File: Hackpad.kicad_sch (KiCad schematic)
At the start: 46 parts, among them Q1 SW_Push, U1 MOUDLE-SEEEDUINO-XIAO

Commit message: Rev 1.0
idk
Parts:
- RGB15: footprint LED_SMD:LED_SK6812MINI_PLCC4_3.5x3.5mm_P1.75mm -> footprints:SK6812MINI-E_fixed
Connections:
- net GND: now also U1.13 (GND)
- net LED: now also U1.8 (PB09_A7_D7_RX); no longer U1.6 (PA9_A5_D5_SCL)
- no-connect marks 0 -> 3
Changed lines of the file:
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@@
 		(color 0 0 0 0)
 	)
+	(no_connect
+		(at 281.94 165.1)
+	)
+	(no_connect
+		(at 21.59 86.36)
+	)
+	(no_connect
+		(at 21.59 83.82)
+	)
 	(wire
 		(pts
@@
 		)
 	)
-	(global_label "LED"
+	(global_label "COL3"
 		(shape input)
-		(at 21.59 83.82 180)
+		(at 132.08 20.32 180)
 		(fields_autoplaced yes)
 		(effects
@@
 		)
 		(property "Intersheetrefs" "${INTERSHEET_REFS}"
-			(at 15.1577 83.82 0)
+			(at 124.2567 20.32 0)
 			(hide yes)
 			(show_name no)
@@
 	(global_label "COL3"
 		(shape input)
-		(at 132.08 20.32 180)
+		(at 21.59 76.2 180)
 		(fields_autoplaced yes)
 		(effects
@@
 		)
 		(property "Intersheetrefs" "${INTERSHEET_REFS}"
-			(at 124.2567 20.32 0)
+			(at 13.7667 76.2 0)
 			(hide yes)
 			(show_name no)
@@
 		)
 	)
-	(global_label "COL3"
+	(global_label "COL4"
 		(shape input)
-		(at 21.59 76.2 180)
+		(at 21.59 78.74 180)
 		(fields_autoplaced yes)
 		(effects
@@
 		)
 		(property "Intersheetrefs" "${INTERSHEET_REFS}"
-			(at 13.7667 76.2 0)
+			(at 13.7667 78.74 0)
 			(hide yes)
 			(show_name no)
@@
 		)
 	)
-	(global_label "COL4"
+	(global_label "ROW1"
 		(shape input)
-		(at 21.59 78.74 180)
+		(at 62.23 76.2 0)
 		(fields_autoplaced yes)
 		(effects
@@
 				(size 1.27 1.27)
 			)
-			(justify right)
+			(justify left)
 		)
 		(property "Intersheetrefs" "${INTERSHEET_REFS}"
-			(at 13.7667 78.74 0)
+			(at 70.4766 76.2 0)
 			(hide yes)
 			(show_name no)
@@
 					(size 1.27 1.27)
 				)
-				(justify right)
+				(justify left)
 			)
 		)
 	)
-	(global_label "ROW1"
+	(global_label "LED"
 		(shape input)
-		(at 62.23 76.2 0)
+		(at 62.23 86.36 0)
 		(fields_autoplaced yes)
 		(effects
@@
 		)
 		(property "Intersheetrefs" "${INTERSHEET_REFS}"
-			(at 70.4766 76.2 0)
+			(at 68.6623 86.36 0)
 			(hide yes)
 			(show_name no)
@@
 			)
 		)
-		(property "Footprint" "LED_SMD:LED_SK6812MINI_PLCC4_3.5x3.5mm_P1.75mm"
+		(property "Footprint" "footprints:SK6812MINI-E_fixed"
 			(at 275.59 172.72 0)
 			(hide yes)
@@
 					(unit 1)
 				)
+			)
+		)
+	)
+	(symbol
+		(lib_id "power:GND")
+		(at 62.23 73.66 90)
+		(unit 1)
+		(body_style 1)
+		(exclude_from_sim no)
+		(in_bom yes)
+		(on_board yes)
+		(in_pos_files yes)
+		(dnp no)
+		(fields_autoplaced yes)
+		(property "Reference" "#PWR032"
+			(at 68.58 73.66 0)
+			(hide yes)
+			(show_name no)
+			(do_not_autoplace no)
+			(effects
+				(font
+					(size 1.27 1.27)
+				)
+			)
+		)
+		(property "Value" "GND"
+			(at 66.04 73.6599 90)
+			(show_name no)
+			(do_not_autoplace no)
+			(effects
+				(font
+					(size 1.27 1.27)
+				)
+				(justify right)
+			)
+		)
+		(property "Footprint" ""
+			(at 62.23 73.66 0)
+			(hide yes)
+			(show_name no)
+			(do_not_autoplace no)
+			(effects
+				(font
+					(size 1.27 1.27)
+				)
+			)
+		)
+		(property "Datasheet" ""
+			(at 62.23 73.66 0)
+			(hide yes)
+			(show_name no)
+			(do_not_autoplace no)
+			(effects
+				(font
+					(size 1.27 1.27)
+				)
+			)
+		)
+		(property "Description" "Power symbol creates a global label with name \"GND\" , ground"
+			(at 62.23 73.66 0)
+			(hide yes)
+			(show_name no)
+			(do_not_autoplace no)
+			(effects
+				(font
+					(size 1.27 1.27)
+				)
+			)
+		)
+		(pin "1"
+		)
+		(instances
+			(project "Hackpad"
+				(path "/c98b0e03-1e76-4efa-b638-77786d3a396d"
+					(reference "#PWR032")
+					(unit 1)
+				)

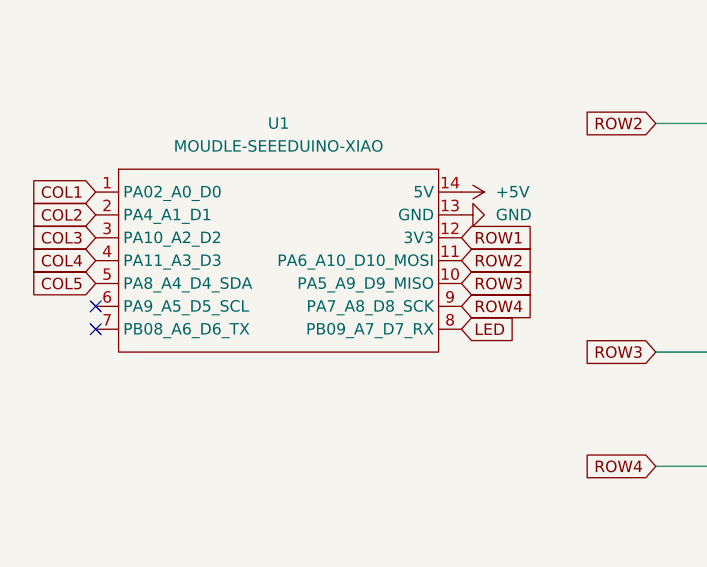
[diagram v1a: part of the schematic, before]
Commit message: 3d model and firmware compiled
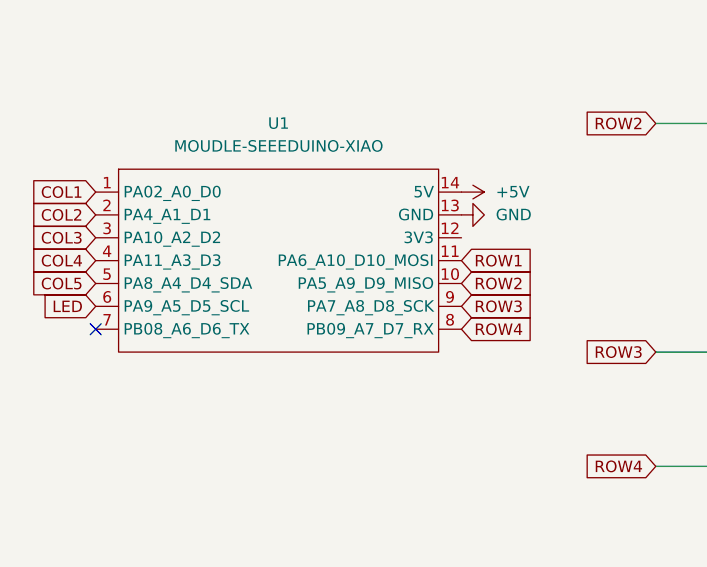
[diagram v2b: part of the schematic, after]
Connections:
- net LED: now also U1.6 (PA9_A5_D5_SCL); no longer U1.8 (PB09_A7_D7_RX)
- net ROW1: now also U1.11 (PA6_A10_D10_MOSI); no longer U1.12 (3V3)
- net ROW2: now also U1.10 (PA5_A9_D9_MISO); no longer U1.11 (PA6_A10_D10_MOSI)
- net ROW3: now also U1.9 (PA7_A8_D8_SCK); no longer U1.10 (PA5_A9_D9_MISO)
- net ROW4: now also U1.8 (PB09_A7_D7_RX); no longer U1.9 (PA7_A8_D8_SCK)
- no-connect marks 3 -> 2
